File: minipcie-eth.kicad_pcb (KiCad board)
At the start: 4 copper layers, 75 x 86 mm, 39 parts, among them J1 Conn_02x03_Odd_Even, J2 PMOD I2C 6pin, J3 Conn_02x03_Odd_Even, J4 PMOD UART 6pin, J5 PMOD UART 6pin, J6 Conn_02x03_Odd_Even, J7 Conn_02x03_Odd_Even, J8 Conn_01x02, U1 VoCore_v2, U2 si3404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

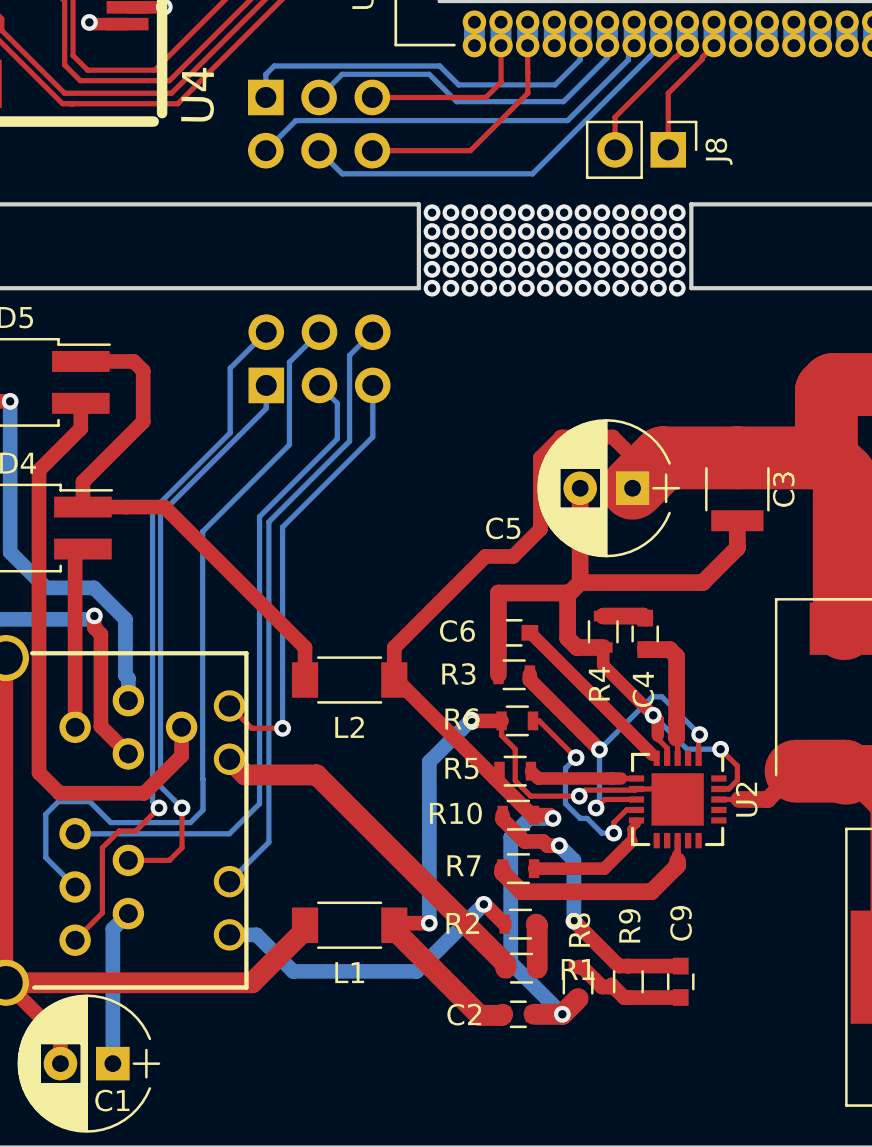
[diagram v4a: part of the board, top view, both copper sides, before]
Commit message: Routing finished, some of the si3404 application notes and via stitching ignored, to revisit later on
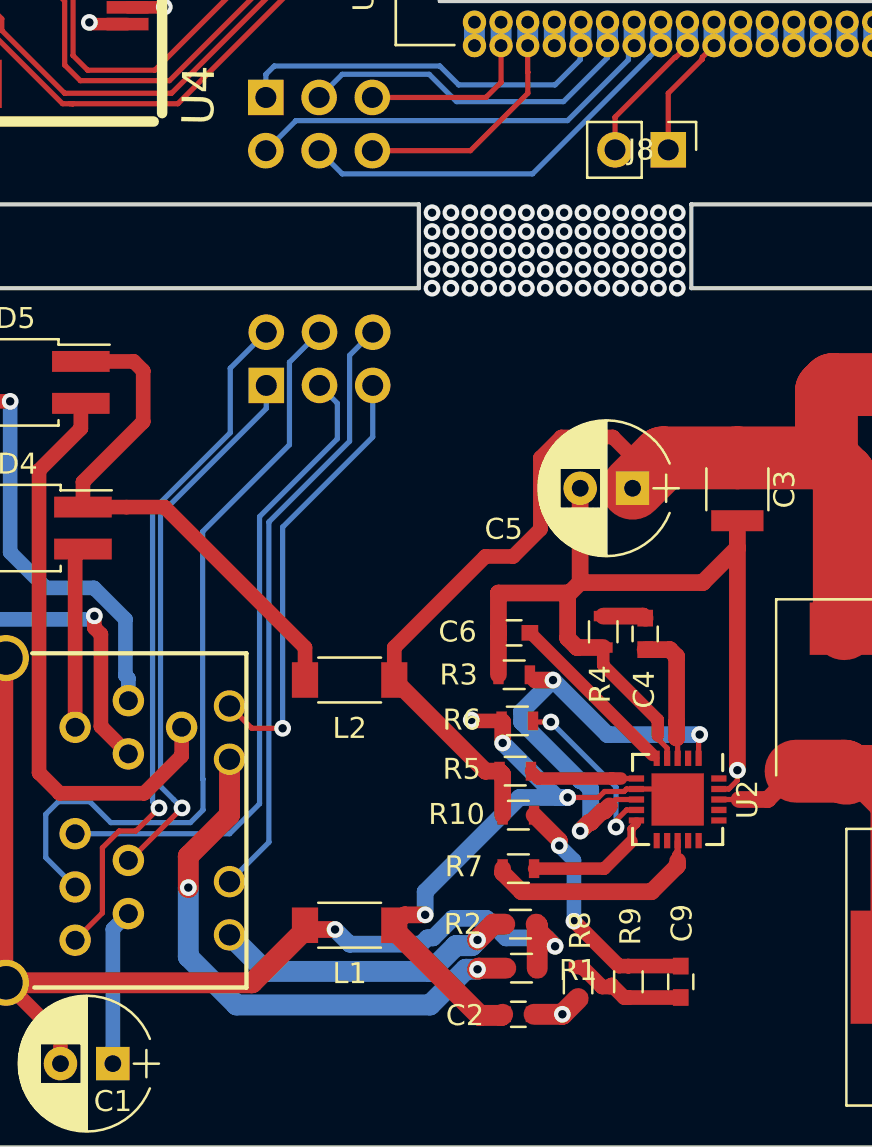
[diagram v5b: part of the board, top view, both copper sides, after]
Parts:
- turned R10 to 0 degrees
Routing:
- net Net-(C1-Pad2): track 63.5 -> 78.3 mm, vias 0 -> 2
- net /ethernet + POE/5V+_POE: track 98.6 -> 85.2 mm, vias 2 -> 1
- net Net-(R1-Pad1): track 17.4 -> 27.1 mm, vias 0 -> 2
- net Net-(R3-Pad2): track 17.6 -> 23.2 mm
- net VSS: track 39.5 -> 44.9 mm, vias 2 -> 1
- net /ethernet + POE/3V3-_POE: track 46.2 -> 44.7 mm
- net Net-(C2-Pad2): track 35.3 -> 34.0 mm, vias 3 -> 4
- net Net-(R6-Pad1): track 9.90 -> 8.66 mm
- net /ethernet + POE/PORP: track 27.4 -> 26.3 mm
- net Net-(R2-Pad1): track 15.6 -> 14.8 mm

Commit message: Some fun with credits and logos
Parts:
- moved J4 0.61 mm to (179.0, 66.8)
- moved J5 0.61 mm to (179.0, 50.0)
- moved J1 0.60 mm to (170.6, 85.8)
- moved J7 0.40 mm to (165.5, 97.3)
- moved J6 0.36 mm to (134.6, 97.3)
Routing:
- net Net-(J4-Pad1): track 40.9 -> 39.8 mm
- net /ethernet + POE/3V3+_POE: track 7.92 -> 7.02 mm
- net Net-(J4-Pad4): track 45.8 -> 45.2 mm
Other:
- board text added: "SiLabs 3404 non-isolated class 2 PoE adapter by brainstorm@nopcode.org"
- board text added: "VoCore2+LoRa+mini-pcie+POE+PMOD by brainstorm@nopcode.org"

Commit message: Add README and some nice pictures
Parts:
- added REF**: OSHW-Logo2_24.3x20mm_SilkScreen, Symbol:OSHW-Logo2_24.3x20mm_SilkScreen, B.Cu at (165.1, 112.8)
- added REF**: OSHW-Logo2_24.3x20mm_SilkScreen, Symbol:OSHW-Logo2_24.3x20mm_SilkScreen, B.Cu at (125.0, 71.8)
- J5: value PMOD UART 6pin -> PMOD GPIO 6pin
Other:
- board text added: "ETH RX/TX"
- board text added: "PMOD GPIO"
- board text added: "PMOD I2C"
- board text added: "PMOD UART"
- board text added: "POE"
- board text added: "VOCORE2 UART"

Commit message: Some minor final tweaks... holes for the standoffs for the minipci-e card are still missing :facepalm:
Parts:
- moved REF** 13.9 mm to (151.2, 112.9)
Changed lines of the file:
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@@
   )
   (module Symbol:OSHW-Logo2_24.3x20mm_SilkScreen (layer B.Cu)
-    (at 165.1 112.799999 180)
+    (at 151.2 112.899999 180)
     (descr "Open Source Hardware Symbol")
     (tags "Logo Symbol OSHW")
